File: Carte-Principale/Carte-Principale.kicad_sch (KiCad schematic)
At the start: 1 part, among them U1 NUCLEOH723ZG

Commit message: Moteurs + Encodeurs
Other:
- sheet Encodeurs ports: added A_DROITE, A_GAUCHE, B_DROITE, B_GAUCHE; removed none
- sheet Moteurs ports: added DIR_MOTEUR_DROITE, DIR_MOTEUR_GAUCHE, EN_MOTEUR_DROIT, EN_MOTEUR_GAUCHE, FAULTDRV, PWM_MOTEUR_DROITE, PWM_MOTEUR_GAUCHE, RSTDRV; removed none
- moved on the sheet: U1E

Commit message: Avancée Actionneur
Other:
- moved on the sheet: U1C, U1D, U1E, U1F

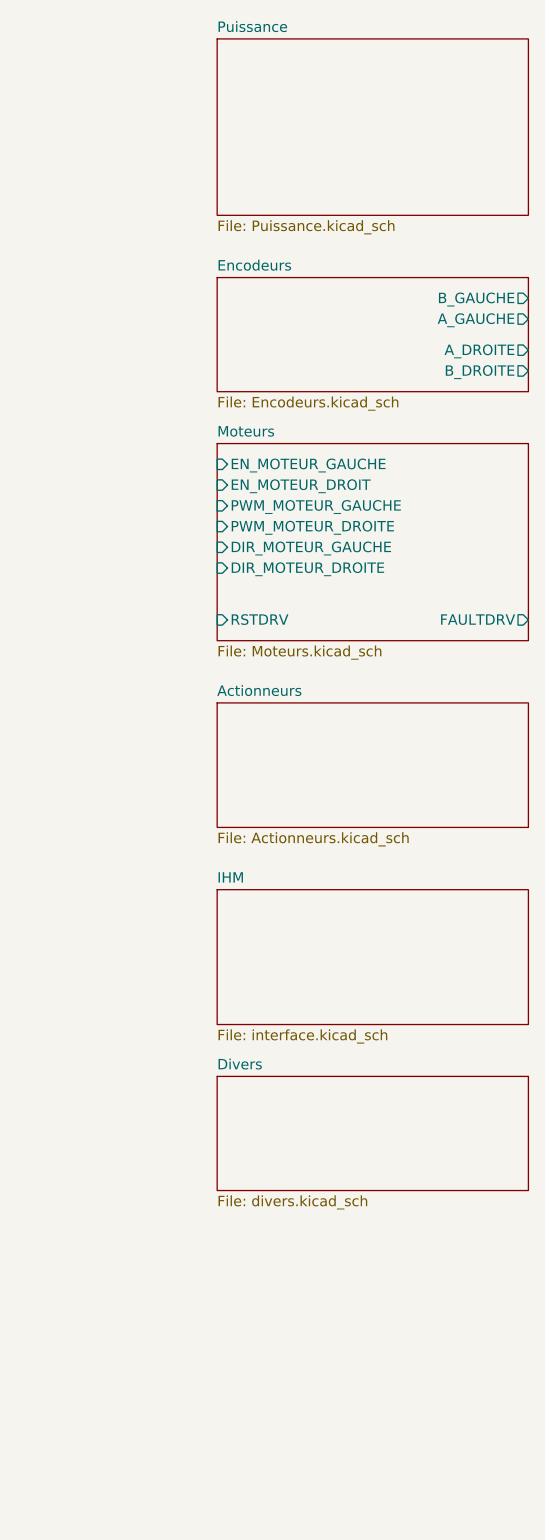
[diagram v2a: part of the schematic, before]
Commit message: Rajout écran
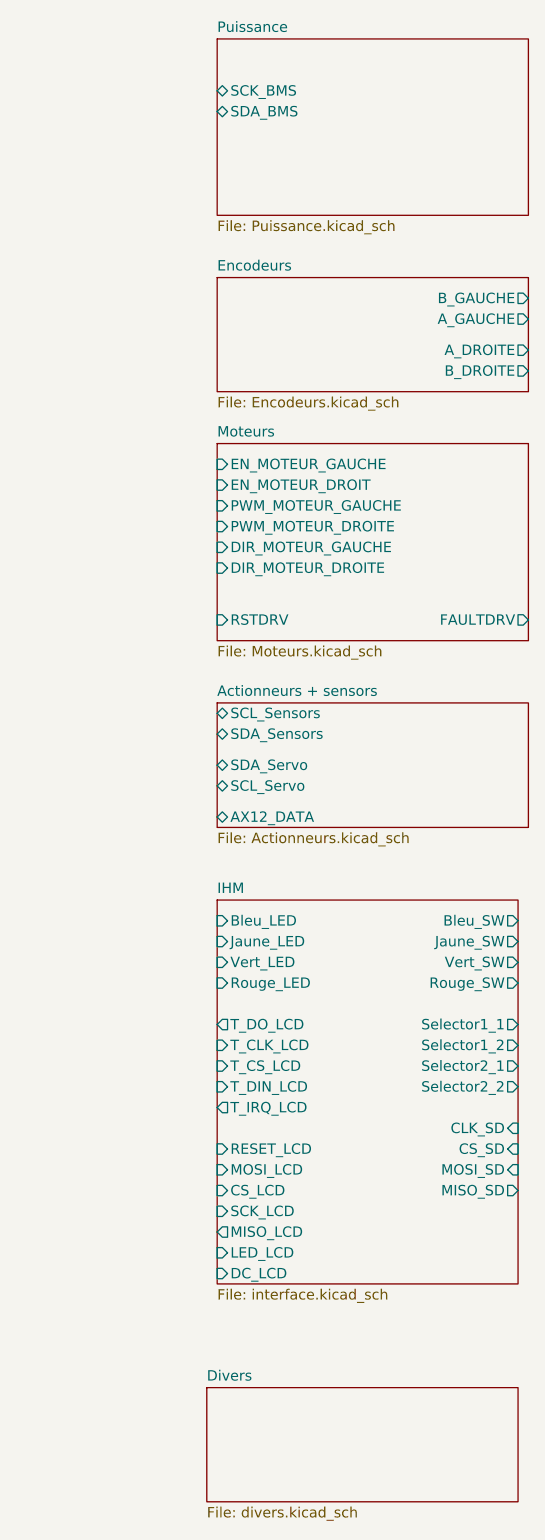
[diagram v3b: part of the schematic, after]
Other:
- sheet Actionneurs renamed Actionneurs + sensors
- sheet Actionneurs + sensors ports: added AX12_DATA, SCL_Sensors, SCL_Servo, SDA_Sensors, SDA_Servo; removed none
- sheet IHM ports: added Bleu_LED, Bleu_SW, CLK_SD, CS_LCD, CS_SD, DC_LCD, Jaune_LED, Jaune_SW, LED_LCD, MISO_LCD, MISO_SD, MOSI_LCD, MOSI_SD, RESET_LCD, Rouge_LED, Rouge_SW, SCK_LCD, Selector1_1, Selector1_2, Selector2_1, Selector2_2, T_CLK_LCD, T_CS_LCD, T_DIN_LCD, T_DO_LCD, T_IRQ_LCD, Vert_LED, Vert_SW; removed none
- sheet Puissance ports: added SCK_BMS, SDA_BMS; removed none

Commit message: wiring
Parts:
- added C1: 0.1uF, Capacitor_SMD:C_1206_3216Metric_Pad1.33x1.80mm_HandSolder, symbol Device:C
- added SW1: RESET, Button_Switch_THT:SW_PUSH_6mm, symbol Switch:SW_Push
- added unit 8 of U1
- added unit 9 of U1
- added unit 10 of U1
- added unit 1 of U1
- added unit 7 of U1
- added unit 2 of U1
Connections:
- net AX12_RX: now reaches U1.CN9_1 (A0/ADC12_INP15)
- net AX12_RX: now also U1.CN9_6 (D53/USART_B_TX), U1.CN11_41 (PD5), U1.CN12_37 (PA3)
- net PD3: now reaches U1.CN9_10 (D55/USART_B_CTS)
- net PD3: now also U1.CN11_40 (PD3)
- net PF10: now reaches U1.CN9_11 (A5/ADC3_INP6/I2C1_SCL)
- net PF10: now also U1.CN12_42 (PF10)
- net GND: now reaches U1.CN9_12 (GND_CN9), U1.CN9_23 (GND_CN9)
- net GND: now also U1.CN10_17 (GND_CN10), U1.CN10_22 (GND_CN10), U1.CN10_27 (GND_CN10), U1.CN10_3 (AGND_CN10), U1.CN10_5 (GND_CN10), U1.CN7_8 (GND_CN7), U1.CN8_11 (GND_CN8), U1.CN8_13 (GND_CN8), C1.2, SW1.1, U1.CN11_19 (GND_CN11), U1.CN11_20 (GND_CN11), U1.CN11_22 (GND_CN11), U1.CN11_49 (GND_CN11), U1.CN11_60 (GND_CN11), U1.CN11_8 (GND_CN11), U1.CN12_20 (GND_CN12), U1.CN12_32 (AGND_CN12), U1.CN12_39 (GND_CN12), U1.CN12_54 (GND_CN12), U1.CN12_63 (GND_CN12), U1.CN12_9 (GND_CN12), U1.CN15_1 (GND_CN15), U1.CN15_2 (GND_CN15), U1.CN16_1 (GND_CN16), U1.CN16_2 (GND_CN16), U1.CN3_1 (GND_CN3), U1.CN3_2 (GND_CN3), U1.CN4_1 (GND_CN4), U1.CN4_2 (GND_CN4)
- net PB2: now reaches U1.CN9_13 (D72/COMP1_INP)
- net PB2: now also U1.CN10_15 (D27/QSPI_CLK), U1.CN12_22 (PB2)
- net PE2: now reaches U1.CN9_14 (D56/SAI_A_MCLK)
- net PE2: now also U1.CN10_25 (D31/QSPI_BK1_IO2), U1.CN11_46 (PE2)
- net PE9: now reaches U1.CN9_15 (D71/COMP2_INP)
- net PE9: now also U1.CN10_4 (D6/TIMER_A_PWM1), U1.CN12_52 (PE9)
- net PE4: now reaches U1.CN9_16 (D57/SAI_A_FS)
- net PE4: now also U1.CN11_48 (PE4)
- net PF2: now reaches U1.CN9_17 (D70/I2C_B_SMBA)
- net PF2: now also U1.CN8_14 (D49/IO), U1.CN11_52 (PF2)
- net PE5: now reaches U1.CN9_18 (D58/SAI_A_SCK)
- net PE5: now also U1.CN11_50 (PE5)
- net I2C2_SCL: now reaches U1.CN9_19 (D69/I2C_B_SCL)
- net I2C2_SCL: now also U1.CN11_51 (PF1)
- net PD7: now reaches U1.CN9_2 (D51/USART_B_SCLK)
- net PD7: now also U1.CN11_45 (PD7)
- net PE6: now reaches U1.CN9_20 (D59/SAI_A_SD)
- net PE6: now also U1.CN10_28 (D38/TIMER_A_BKIN2), U1.CN11_62 (PE6)
- net I2C2_SDA: now reaches U1.CN9_21 (D68/I2C_B_SDA)
- net I2C2_SDA: now also U1.CN11_53 (PF0)
- net PE3: now reaches U1.CN9_22 (D60/SAI_B_SD)
- net PE3: now also U1.CN11_47 (PE3)
- net PF8: now reaches U1.CN9_24 (D61/SAI_B_SCK)
- net PF8: now also U1.CN11_54 (PF8)
- net PD0: now reaches U1.CN9_25 (D67/CAN_RX)
- net PD0: now also U1.CN11_57 (PD0)
- net Encodeur_Droit_B: now reaches U1.CN9_26 (D62/SAI_B_MCLK)
- net Encodeur_Droit_B: now also U1.CN11_11 (PF7)
- net PD1: now reaches U1.CN9_27 (D66/CAN_TX)
- net PD1: now also U1.CN11_55 (PD1)
- net PF9: now reaches U1.CN9_28 (D63/SAI_B_FS)
- net PF9: now also U1.CN11_56 (PF9)
- net PG0: now reaches U1.CN9_29 (D65/IO)
- net PG0: now also U1.CN11_59 (PG0)
- net PC0: now reaches U1.CN9_3 (A1/ADC123_INP10)
- net PC0: now also U1.CN11_38 (PC0)
- net PG1: now reaches U1.CN9_30 (D64/IO)
- net PG1: now also U1.CN11_58 (PG1)
- net PD6: now reaches U1.CN9_4 (D52/USART_B_RX)
- net PD6: now also U1.CN11_43 (PD6)
- net PC3: now reaches U1.CN9_5 (A2/ADC12_INP13)
- net PC3: now also U1.CN11_37 (PC3)
- net PB1: now reaches U1.CN9_7 (A3/ADC12_INP5)
- net PB1: now also U1.CN12_24 (PB1)
- net PD4: now reaches U1.CN9_8 (D54/USART_B_RTS)
- net PD4: now also U1.CN11_39 (PD4)
- net PC2: now reaches U1.CN9_9 (A4/ADC123_INP12/I2C1_SDA)
- net PC2: now also U1.CN11_35 (PC2)
- net PC12: now reaches U1.CN8_10 (D47/SDMMC_CK)
- net PC12: now also U1.CN11_3 (PC12)
- net PD2: now reaches U1.CN8_12 (D48/SDMMC_CMD)
- net PD2: now also U1.CN11_4 (PD2)
- net PG3: now reaches U1.CN8_16 (D50/IO)
- net PG3: now also U1.CN11_44 (PG3)
- net PC8: now reaches U1.CN8_2 (D43/SDMMC_D0)
- net PC8: now also U1.CN12_2 (PC8)
- net I2C3_SDA: now reaches U1.CN8_4 (D44/SDMMC_D1/I2S_A_CKIN)
- net I2C3_SDA: now also U1.CN12_1 (PC9)
- net NRST: now reaches U1.CN8_5 (NRST_CN8)
- net NRST: now also C1.1, SW1.2, U1.CN11_14 (NRST)
- net PC10: now reaches U1.CN8_6 (D45/SDMMC_D2)
- net PC10: now also U1.CN11_1 (PC10)
- net +3V3: now reaches U1.CN8_7 (3V3_CN8)
- net +3V3: now also U1.CN11_16 (3V3)
- net PC11: now reaches U1.CN8_8 (D46/SDMMC_D3)
- net PC11: now also U1.CN11_2 (PC11)
- net PC6: now reaches U1.CN7_1 (D16/I2S_A_MCK)
- net PC6: now also U1.CN12_4 (PC6)
- net PA5: now reaches U1.CN7_10 (D13/SPI_A_SCK)
- net PA5: now also U1.CN12_11 (PA5)
- net PC7: now reaches U1.CN7_11 (D21/I2S_B_MCK)
- net PC7: now also U1.CN12_19 (PC7)
- net PA6: now reaches U1.CN7_12 (D12/SPI_A_MISO)
- net PA6: now also U1.CN12_13 (PA6)
- net PB5: now reaches U1.CN7_13 (D22/I2S_B_SD/SPI_B_MOSI)
- net PB5: now also U1.CN7_14 (D11/SPI_A_MOSI/TIM_E_PWM1), U1.CN12_29 (PB5)
- net PB3: now reaches U1.CN7_15 (D23/I2S_B_CK/SPI_B_SCK)
- net PD14: now reaches U1.CN7_16 (D10/SPI_A_CS/TIM_B_PWM3)
- net PD14: now also U1.CN12_46 (PD14)
- net PA4: now reaches U1.CN7_17 (D24/SPI_B_NSS)
- net PA4: now also U1.CN11_32 (PA4)
- net PD15: now reaches U1.CN7_18 (D9/TIMER_B_PWM2)
- net PD15: now also U1.CN12_48 (PD15)
- net PB4: now reaches U1.CN7_19 (D25/SPI_B_MISO)
- net PB4: now also U1.CN12_27 (PB4)
- net PB8: now reaches U1.CN7_2 (D15/I2C_A_SCL)
- net PB8: now also U1.CN12_3 (PB8)
- net PF3: now reaches U1.CN7_20 (D8/IO)
- net PF3: now also U1.CN12_58 (PF3)
- net PB15: now reaches U1.CN7_3 (D17/I2S_A_SD)
- net PB15: now also U1.CN12_26 (PB15)
- net PB9: now reaches U1.CN7_4 (D14/I2C_A_SDA)
- net PB9: now also U1.CN12_5 (PB9)
- net PB13: now reaches U1.CN7_5 (D18/I2S_A_CK)
- net PB13: now also U1.CN12_30 (PB13)
- net PB12: now reaches U1.CN7_7 (D19/I2S_A_WS)
- net PB12: now also U1.CN12_16 (PB12)
- net PA15: now reaches U1.CN7_9 (D20/I2S_B_WS)
- net PA15: now also U1.CN11_17 (PA15)
- net PE13: now reaches U1.CN10_10 (D3/TIMER_A_PWM3)
- net PE13: now also U1.CN12_55 (PE13)
- net Encodeur_Droit_A: now reaches U1.CN10_11 (A8/ADC_C_IN)
- net Encodeur_Droit_A: now also U1.CN11_9 (PF6)
- net PG14: now reaches U1.CN10_12 (D2/IO)
- net PG14: now also U1.CN12_61 (PG14)
- net PG6: now reaches U1.CN10_13 (D26/QSPI_CS)
- net PG6: now also U1.CN12_70 (PG6)
- net I2C1_SCL: now reaches U1.CN10_14 (D1/USART_A_TX)
- net I2C1_SCL: now also U1.CN12_17 (PB6)
- net I2C1_SDA: now reaches U1.CN10_16 (D0/USART_A_RX)
- net I2C1_SDA: now also U1.CN11_21 (PB7)
- net PE8: now reaches U1.CN10_18 (D42/TIMER_A_PWM1N)
- net PE8: now also U1.CN12_40 (PE8)
- net PD13: now reaches U1.CN10_19 (D28/QSPI_BK1_IO3)
- net PD13: now also U1.CN12_41 (PD13)
- net PG12: now reaches U1.CN10_2 (D7/IO)
- net PG12: now also U1.CN11_65 (PG12)
- net PE7: now reaches U1.CN10_20 (D41/TIMER_A_ETR)
- net PE7: now also U1.CN12_44 (PE7)
- net PD12: now reaches U1.CN10_21 (D29/QSPI_BK1_IO1)
- net PD12: now also U1.CN12_43 (PD12)
- net PD11: now reaches U1.CN10_23 (D30/QSPI_BK1_IO0)
- net PD11: now also U1.CN12_45 (PD11)
- net PE10: now reaches U1.CN10_24 (D40/TIMER_A_PWM2N)
- net PE10: now also U1.CN12_47 (PE10)
- net PE12: now reaches U1.CN10_26 (D39/TIMER_A_PWM3N)
- net PE12: now also U1.CN12_49 (PE12)
- net PA0: now reaches U1.CN10_29 (D32/TIMER_C_PWM1)
- net PA0: now also U1.CN11_28 (PA0)
- net PE15: now reaches U1.CN10_30 (D37/TIMER_A_BKIN1)
- net PE15: now also U1.CN12_53 (PE15)
- net PB0: now reaches U1.CN10_31 (D33/TIMER_D_PWM1)
- net PB10: now reaches U1.CN10_32 (D36/TIMER_C_PWM2)
- net PB10: now also U1.CN12_25 (PB10)
- net PB11: now reaches U1.CN10_34 (D35/TIMER_C_PWM3)
- net PB11: now also U1.CN12_18 (PB11)
- net PE11: now reaches U1.CN10_6 (D5/TIMER_A_PWM2)
- net PE11: now also U1.CN12_56 (PE11)
- net PF4: now reaches U1.CN10_7 (A6/ADC_A_IN)
- net PF4: now also U1.CN12_38 (PF4)
- net PE14: now reaches U1.CN10_8 (D4/IO)
- net PE14: now also U1.CN12_51 (PE14)
- net PF5: now reaches U1.CN10_9 (A7/ADC_B_IN)
- net PF5: now also U1.CN12_36 (PF5)
- new net: U1.CN11_10 (NC), U1.CN11_26 (NC), U1.CN11_67 (NC)
- new net DEBUG_RX: U1.CN11_69 (PD9)
- new net DEBUG_TX: U1.CN12_10 (PD8)
- new net Encodeur_Gauche_A: U1.CN12_62 (PF11)
- new net Encodeur_Gauche_B: U1.CN12_59 (PF12)
- new net I2C3_SCL: U1.CN12_23 (PA8)
- new net PA10: U1.CN12_33 (PA10)
- new net PA11: U1.CN12_14 (PA11)
- new net PA12: U1.CN12_12 (PA12)
- new net PA9: U1.CN12_21 (PA9)
- new net PB14: U1.CN12_28 (PB14)
- new net PE0: U1.CN12_64 (PE0)
- new net PF13: U1.CN12_57 (PF13)
- new net PF14: U1.CN12_50 (PF14)
- new net PF15: U1.CN12_60 (PF15)
- new net PG10: U1.CN11_66 (PG10)
- new net PG15: U1.CN11_64 (PG15)
- new net PG2: U1.CN11_42 (PG2)
- new net PG4: U1.CN12_69 (PG4)
- new net PG5: U1.CN12_68 (PG5)
- new net PG8: U1.CN12_66 (PG8)
- new net PG9: U1.CN11_63 (PG9)
- no-connect marks 0 -> 37
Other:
- sheet Actionneurs + sensors ports: added IT_Ready_Sensors; removed none
- sheet IHM ports: added SCK_SD, T_MISO_LCD, T_MOSI_LCD, T_SCK_LCD; removed CLK_SD, LED_LCD, Selector1_1, Selector1_2, Selector2_1, Selector2_2, T_CLK_LCD, T_DIN_LCD, T_DO_LCD
- sheet Moteurs ports: added PWM_MOTEUR_DROITE_H, PWM_MOTEUR_GAUCHE_H; removed PWM_MOTEUR_DROITE, PWM_MOTEUR_GAUCHE
- sheet Puissance ports: added none; removed SCK_BMS, SDA_BMS
- note added: "Alimenté via USB"
- note added: "TIM23 -> Encodeur Droit TIM24 -> Encodeur Gauche TIM1 -> PWM Moteurs USART2 -> AX12 USART3 -> Debug + Serial console I2C1 -> Sensors + Servos SPI1 -> LCD + Touch + SD PF2 -> EXTI2 Touch PF3 -> EXTI3 Sensors"

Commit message: Schéma vérifié
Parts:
- added F1: 1.3A, Fuse:Fuse_2010_5025Metric_Pad1.52x2.65mm_HandSolder, symbol Device:Polyfuse
- added H1, H2, H3, H4: MountingHole, MountingHole:MountingHole_3.2mm_M3, symbol Mechanical:MountingHole
- added J1: Serial, Connector_Molex:Molex_KK-254_AE-6410-03A_1x03_P2.54mm_Vertical, symbol Connector:Conn_01x03_Pin
- added J2: PA, Connector_Molex:Molex_KK-254_AE-6410-05A_1x05_P2.54mm_Vertical, symbol Connector:Conn_01x05_Pin
- added J3: PG, Connector_Molex:Molex_KK-254_AE-6410-08A_1x08_P2.54mm_Vertical, symbol Connector:Conn_01x08_Pin
- added J4: SPI2, Connector_Molex:Molex_KK-254_AE-6410-04A_1x04_P2.54mm_Vertical, symbol Connector:Conn_01x04_Pin
- added J5: SPI3, Connector_Molex:Molex_KK-254_AE-6410-04A_1x04_P2.54mm_Vertical, symbol Connector:Conn_01x04_Pin
- added J6: I2C2, Connector_Molex:Molex_KK-254_AE-6410-03A_1x03_P2.54mm_Vertical, symbol Connector:Conn_01x03_Pin
- added J7: I2C3, Connector_Molex:Molex_KK-254_AE-6410-03A_1x03_P2.54mm_Vertical, symbol Connector:Conn_01x03_Pin
- C1: footprint Capacitor_SMD:C_1206_3216Metric_Pad1.33x1.80mm_HandSolder -> Capacitor_SMD:C_1210_3225Metric_Pad1.33x2.70mm_HandSolder
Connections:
- net +3V3: now also F1.2; no longer U1.CN11_16 (3V3)
- net DEBUG_RX: now also J1.3 (Pin_3)
- net DEBUG_TX: now also J1.2 (Pin_2)
- net GND: now also J1.1 (Pin_1), J2.1 (Pin_1), J3.1 (Pin_1), J4.1 (Pin_1), J5.1 (Pin_1), J6.1 (Pin_1), J7.1 (Pin_1)
- net I2C2_SCL: now also J6.3 (Pin_3)
- net I2C2_SDA: now also J6.2 (Pin_2)
- net I2C3_SCL: now also J7.3 (Pin_3)
- net I2C3_SDA: now also J7.2 (Pin_2)
- net PA10: now also J2.4 (Pin_4)
- net PA11: now also J2.3 (Pin_3)
- net PA12: now also J2.2 (Pin_2)
- net PA9: now also J2.5 (Pin_5)
- net PB10: now also J4.4 (Pin_4)
- net PB2: now also J5.2 (Pin_2)
- net PC10: now also J5.4 (Pin_4)
- net PC11: now also J5.3 (Pin_3)
- net PC2: now also J4.3 (Pin_3)
- net PC3: now also J4.2 (Pin_2)
- net PE0: now also U1.CN10_33 (D34/TIMER_B_ETR)
- net PF2: no longer U1.CN8_14 (D49/IO)
- net PG10: now also J3.3 (Pin_3)
- net PG15: now also J3.2 (Pin_2)
- net PG2: now also U1.CN8_14 (D49/IO), J3.8 (Pin_8)
- net PG4: now also J3.7 (Pin_7)
- net PG5: now also J3.6 (Pin_6)
- net PG8: now also J3.5 (Pin_5)
- net PG9: now also J3.4 (Pin_4)
- net PB0: no longer names the net of U1.CN10_31 (D33/TIMER_D_PWM1)
- net PB3: no longer names the net of U1.CN7_15 (D23/I2S_B_CK/SPI_B_SCK)
- net PB4: no longer names the net of U1.CN7_19 (D25/SPI_B_MISO)
- net PB4: no longer U1.CN12_27 (PB4)
- new net: F1.1, U1.CN11_16 (3V3)
- no-connect marks 37 -> 39
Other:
- removed sheet Divers
- note added: "Bien Def Pull Down"
- note added: "PA utilisé pour USB FS"
- company: (none) -> CRINSA
- title: (none) -> Carte Principale

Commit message: Avancée PCB
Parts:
- removed C1: 0.1uF, Capacitor_SMD:C_1210_3225Metric_Pad1.33x2.70mm_HandSolder, symbol Device:C
- removed J2: PA, Connector_Molex:Molex_KK-254_AE-6410-05A_1x05_P2.54mm_Vertical, symbol Connector:Conn_01x05_Pin
- removed J3: PG, Connector_Molex:Molex_KK-254_AE-6410-08A_1x08_P2.54mm_Vertical, symbol Connector:Conn_01x08_Pin
- removed SW1: RESET, Button_Switch_THT:SW_PUSH_6mm, symbol Switch:SW_Push
- renumbered J4 to J2, J5 to J3, J6 to J4, J7 to J5
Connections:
- net PA0: no longer U1.CN11_28 (PA0)
- net PA10: no longer U1.CN12_33 (PA10)
- net PA11: no longer U1.CN12_14 (PA11)
- net PA12: no longer U1.CN12_12 (PA12)
- net PA15: no longer U1.CN11_17 (PA15)
- net PA4: no longer U1.CN11_32 (PA4)
- net PA5: no longer U1.CN12_11 (PA5)
- net PA6: no longer U1.CN12_13 (PA6)
- net PA9: no longer U1.CN12_21 (PA9)
- net PB1: no longer U1.CN12_24 (PB1)
- net PB10: no longer U1.CN12_25 (PB10)
- net PB11: no longer U1.CN12_18 (PB11)
- net PB12: no longer U1.CN12_16 (PB12)
- net PB13: no longer U1.CN12_30 (PB13)
- net PB14: no longer U1.CN12_28 (PB14)
- net PB15: no longer U1.CN12_26 (PB15)
- net PB2: no longer U1.CN12_22 (PB2)
- net PB5: no longer U1.CN12_29 (PB5)
- net PB8: no longer U1.CN12_3 (PB8)
- net PB9: no longer U1.CN12_5 (PB9)
- net PC0: no longer U1.CN11_38 (PC0)
- net PC10: no longer U1.CN11_1 (PC10)
- net PC11: no longer U1.CN11_2 (PC11)
- net PC12: no longer U1.CN11_3 (PC12)
- net PC2: no longer U1.CN11_35 (PC2)
- net PC3: no longer U1.CN11_37 (PC3)
- net PC6: no longer U1.CN12_4 (PC6)
- net PC7: no longer U1.CN12_19 (PC7)
- net PC8: no longer U1.CN12_2 (PC8)
- net PD0: no longer U1.CN11_57 (PD0)
- net PD1: no longer U1.CN11_55 (PD1)
- net PD11: no longer U1.CN12_45 (PD11)
- net PD12: no longer U1.CN12_43 (PD12)
- net PD13: no longer U1.CN12_41 (PD13)
- net PD14: no longer U1.CN12_46 (PD14)
- net PD15: no longer U1.CN12_48 (PD15)
- net PD2: no longer U1.CN11_4 (PD2)
- net PD3: no longer U1.CN11_40 (PD3)
- net PD4: no longer U1.CN11_39 (PD4)
- net PD6: no longer U1.CN11_43 (PD6)
- net PD7: no longer U1.CN11_45 (PD7)
- net PE0: no longer U1.CN12_64 (PE0)
- net PE10: no longer U1.CN12_47 (PE10)
- net PE11: no longer U1.CN12_56 (PE11)
- net PE12: no longer U1.CN12_49 (PE12)
- net PE13: no longer U1.CN12_55 (PE13)
- net PE14: no longer U1.CN12_51 (PE14)
- net PE15: no longer U1.CN12_53 (PE15)
- net PE2: no longer U1.CN11_46 (PE2)
- net PE3: no longer U1.CN11_47 (PE3)
- net PE4: no longer U1.CN11_48 (PE4)
- net PE5: no longer U1.CN11_50 (PE5)
- net PE6: no longer U1.CN11_62 (PE6)
- net PE7: no longer U1.CN12_44 (PE7)
- net PE8: no longer U1.CN12_40 (PE8)
- net PE9: no longer U1.CN12_52 (PE9)
- net PF10: no longer U1.CN12_42 (PF10)
- net PF13: no longer U1.CN12_57 (PF13)
- net PF14: no longer U1.CN12_50 (PF14)
- net PF15: no longer U1.CN12_60 (PF15)
- net PF2: no longer U1.CN11_52 (PF2)
- net PF3: no longer U1.CN12_58 (PF3)
- net PF4: no longer U1.CN12_38 (PF4)
- net PF5: no longer U1.CN12_36 (PF5)
- net PF8: no longer U1.CN11_54 (PF8)
- net PF9: no longer U1.CN11_56 (PF9)
- net PG0: no longer U1.CN11_59 (PG0)
- net PG1: no longer U1.CN11_58 (PG1)
- net PG10: no longer U1.CN11_66 (PG10)
- net PG12: no longer U1.CN11_65 (PG12)
- net PG14: no longer U1.CN12_61 (PG14)
- net PG15: no longer U1.CN11_64 (PG15)
- net PG2: no longer U1.CN11_42 (PG2)
- net PG3: no longer U1.CN11_44 (PG3)
- net PG4: no longer U1.CN12_69 (PG4)
- net PG5: no longer U1.CN12_68 (PG5)
- net PG6: no longer U1.CN12_70 (PG6)
- net PG8: no longer U1.CN12_66 (PG8)
- net PG9: no longer U1.CN11_63 (PG9)
- net at F1.1, U1.CN11_16 (3V3): now also U1.CN8_7 (3V3_CN8)
- net +3V3 renamed +3.3V
- net +3.3V: no longer U1.CN8_7 (3V3_CN8)
- net NRST: no longer names the net of U1.CN8_5 (NRST_CN8)
- net NRST: no longer U1.CN11_14 (NRST)
- no-connect marks 39 -> 163
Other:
- note added: "Utilisé pour USB FS"
- note removed: "PA utilisé pour USB FS"
- moved on the sheet: J1

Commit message: avancée
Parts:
- removed F1: 1.3A, Fuse:Fuse_2010_5025Metric_Pad1.52x2.65mm_HandSolder, symbol Device:Polyfuse
- removed J1: Serial, Connector_Molex:Molex_KK-254_AE-6410-03A_1x03_P2.54mm_Vertical, symbol Connector:Conn_01x03_Pin
- removed J3: SPI3, Connector_Molex:Molex_KK-254_AE-6410-04A_1x04_P2.54mm_Vertical, symbol Connector:Conn_01x04_Pin
- removed J4: I2C2, Connector_Molex:Molex_KK-254_AE-6410-03A_1x03_P2.54mm_Vertical, symbol Connector:Conn_01x03_Pin
- removed J5: I2C3, Connector_Molex:Molex_KK-254_AE-6410-03A_1x03_P2.54mm_Vertical, symbol Connector:Conn_01x03_Pin
- added F3: 1.3A, Fuse:Fuse_2010_5025Metric_Pad1.52x2.65mm_HandSolder, symbol Device:Polyfuse
- added J10: SPI3, Connector_Molex:Molex_KK-254_AE-6410-04A_1x04_P2.54mm_Vertical, symbol Connector:Conn_01x04_Pin
- added J11: GPIO, Connector_Molex:Molex_KK-254_AE-6410-04A_1x04_P2.54mm_Vertical, symbol Connector:Conn_01x04_Pin
- added J5: UART_Debug, Connector_Molex:Molex_KK-254_AE-6410-04A_1x04_P2.54mm_Vertical, symbol Connector:Conn_01x04_Pin
- added J6: UART, Connector_Molex:Molex_KK-254_AE-6410-04A_1x04_P2.54mm_Vertical, symbol Connector:Conn_01x04_Pin
- added J8: I2C2, Connector_Molex:Molex_KK-254_AE-6410-04A_1x04_P2.54mm_Vertical, symbol Connector:Conn_01x04_Pin
- J9: renamed from J2; value SPI2 -> GPIO
- renumbered H3 to H1, H4 to H2, H1 to H3, H2 to H4, U1 to U2
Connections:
- net +3.3V: now also F3.2
- net AX12_RX: no longer U2.CN9_1 (A0/ADC12_INP15), U2.CN9_6 (D53/USART_B_TX)
- net DEBUG_RX: now also J5.1 (Pin_1)
- net DEBUG_TX: now also J5.2 (Pin_2)
- net Encodeur_Droit_A: no longer U2.CN10_11 (A8/ADC_C_IN)
- net Encodeur_Droit_B: no longer U2.CN9_26 (D62/SAI_B_MCLK)
- net GND: now also J10.4 (Pin_4), J5.4 (Pin_4), J6.4 (Pin_4), J8.4 (Pin_4); no longer J9.1 (Pin_1)
- net I2C1_SCL: no longer U2.CN10_14 (D1/USART_A_TX)
- net I2C1_SDA: no longer U2.CN10_16 (D0/USART_A_RX)
- net I2C2_SCL: now also J8.1 (Pin_1); no longer U2.CN11_51 (PF1)
- net I2C2_SDA: now also J8.2 (Pin_2); no longer U2.CN11_53 (PF0)
- net PB10: no longer J9.4 (Pin_4)
- net PB2: now also J10.1 (Pin_1); no longer U2.CN10_15 (D27/QSPI_CLK)
- net PC10: now also J10.3 (Pin_3)
- net PC11: now also J10.2 (Pin_2)
- net PC6: now also J6.2 (Pin_2)
- net PC7: now also J6.1 (Pin_1)
- net PD1: now also J9.4 (Pin_4)
- net PD3: now also J11.1 (Pin_1)
- net PD6: now also J11.2 (Pin_2)
- net PE2: no longer U2.CN10_25 (D31/QSPI_BK1_IO2)
- net PE6: no longer U2.CN9_20 (D59/SAI_A_SD)
- net PE9: no longer U2.CN9_15 (D71/COMP2_INP)
- net PF8: now also J9.1 (Pin_1)
- net PF9: now also J11.4 (Pin_4)
- net PG0: now also J9.3 (Pin_3)
- net PG1: now also J9.2 (Pin_2)
- net at U2.CN8_7 (3V3_CN8): now also F3.1; no longer U2.CN11_16 (3V3)
- net I2C3_SCL: no longer names the net of U2.CN12_23 (PA8)
- net I2C3_SDA: no longer names the net of U2.CN12_1 (PC9)
- net I2C3_SDA: no longer U2.CN8_4 (D44/SDMMC_D1/I2S_A_CKIN)
- net PB1: no longer names the net of U2.CN9_7 (A3/ADC12_INP5)
- net PB5: no longer names the net of U2.CN7_13 (D22/I2S_B_SD/SPI_B_MOSI)
- net PB5: no longer U2.CN7_14 (D11/SPI_A_MOSI/TIM_E_PWM1)
- net PB8: no longer names the net of U2.CN7_2 (D15/I2C_A_SCL)
- net PB9: no longer names the net of U2.CN7_4 (D14/I2C_A_SDA)
- net PC0: no longer names the net of U2.CN9_3 (A1/ADC123_INP10)
- net PC2: no longer names the net of U2.CN9_9 (A4/ADC123_INP12/I2C1_SDA)
- net PC2: no longer J9.3 (Pin_3)
- net PC3: no longer names the net of U2.CN9_5 (A2/ADC12_INP13)
- net PC3: no longer J9.2 (Pin_2)
- net PD14: no longer names the net of U2.CN7_16 (D10/SPI_A_CS/TIM_B_PWM3)
- net PD15: no longer names the net of U2.CN7_18 (D9/TIMER_B_PWM2)
- net PE13: no longer names the net of U2.CN10_10 (D3/TIMER_A_PWM3)
- net PE14: no longer names the net of U2.CN10_8 (D4/IO)
- net PF10: no longer names the net of U2.CN9_11 (A5/ADC3_INP6/I2C1_SCL)
- net PG12: no longer names the net of U2.CN10_2 (D7/IO)
- net PG14: no longer names the net of U2.CN10_12 (D2/IO)
- new net +5V: J5.3 (Pin_3), J6.3 (Pin_3), J8.3 (Pin_3)
- new net PC9: U2.CN8_4 (D44/SDMMC_D1/I2S_A_CKIN)
- new net PD5: U2.CN9_6 (D53/USART_B_TX)
- new net PF6: U2.CN10_11 (A8/ADC_C_IN)
- new net PF7: J11.3 (Pin_3), U2.CN9_26 (D62/SAI_B_MCLK)
- no-connect marks 163 -> 162
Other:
- note removed: "Utilisé pour USB FS"
- moved on the sheet: J9

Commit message: Final pcb modification
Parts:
- added J2: GND, Connector_PinHeader_2.54mm:PinHeader_1x04_P2.54mm_Vertical, symbol Connector:Conn_01x04_Pin
- renumbered J9 to J10, J8 to J11, J11 to J12, J5 to J6, J6 to J7, J10 to J9
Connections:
- net GND: now also J2.1 (Pin_1), J2.2 (Pin_2), J2.3 (Pin_3), J2.4 (Pin_4)
- no-connect marks 162 -> 161
